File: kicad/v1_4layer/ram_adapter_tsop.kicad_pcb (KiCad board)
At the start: 4 copper layers, 17.8 x 40.6 mm, 5 parts, among them J1 Conn_01x16_Male, J2 Conn_01x16_Male, U1 IS61C5128AL-10KLI

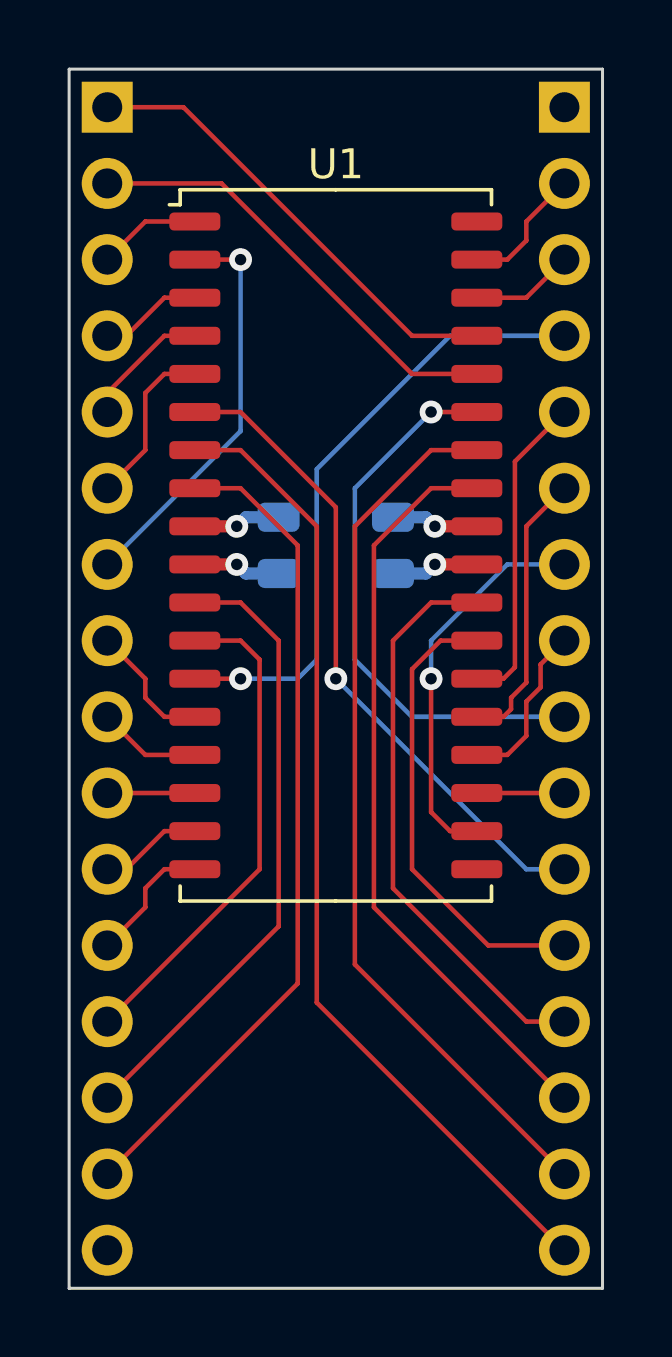
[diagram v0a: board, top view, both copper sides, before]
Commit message: Updated to 8/8 and 26/12 VIAs
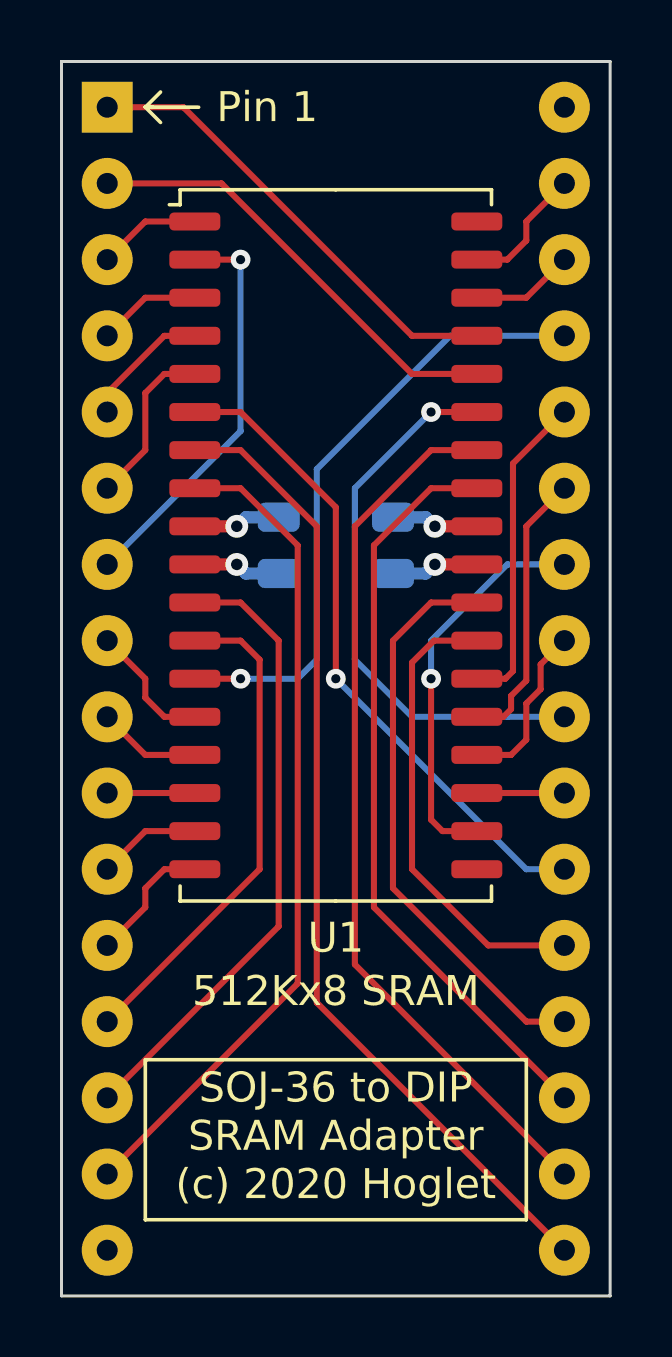
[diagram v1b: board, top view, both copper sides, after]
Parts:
- J1: footprint Connector_PinHeader_2.54mm:PinHeader_1x16_P2.54mm_Vertical -> footprints:PinHeader_1x16_P2.54mm_Vertical
- J2: footprint Connector_PinHeader_2.54mm:PinHeader_1x16_P2.54mm_Vertical -> footprints:PinHeader_1x16_P2.54mm_VerticalAllRound
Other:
- board size 17.8 x 40.6 mm -> 18.3 x 41.1 mm
- net class Default: clearance 0.1524 -> 0.2032; trace_width 0.1524 -> 0.2032; via_dia 0.762 -> 0.6604; via_drill 0.381 -> 0.3048
- rule trace_clearance: 0.1524 -> 0.2032
- rule trace_min: 0.1524 -> 0.2032
- rule via_min_drill: 0.381 -> 0.3048
- rule via_min_size: 0.762 -> 0.6096
- board text added: "512Kx8 SRAM"
- board text added: "Pin 1"
- board text added: "SOJ-36 to DIP SRAM Adapter (c) 2020 Hoglet"
